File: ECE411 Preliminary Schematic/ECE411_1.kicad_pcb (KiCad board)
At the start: 2 copper layers, 12 parts, among them J2 Raspberry_Pi_4, M1 Motor_Servo, U1 XVF3800 (XM-014888-PC)

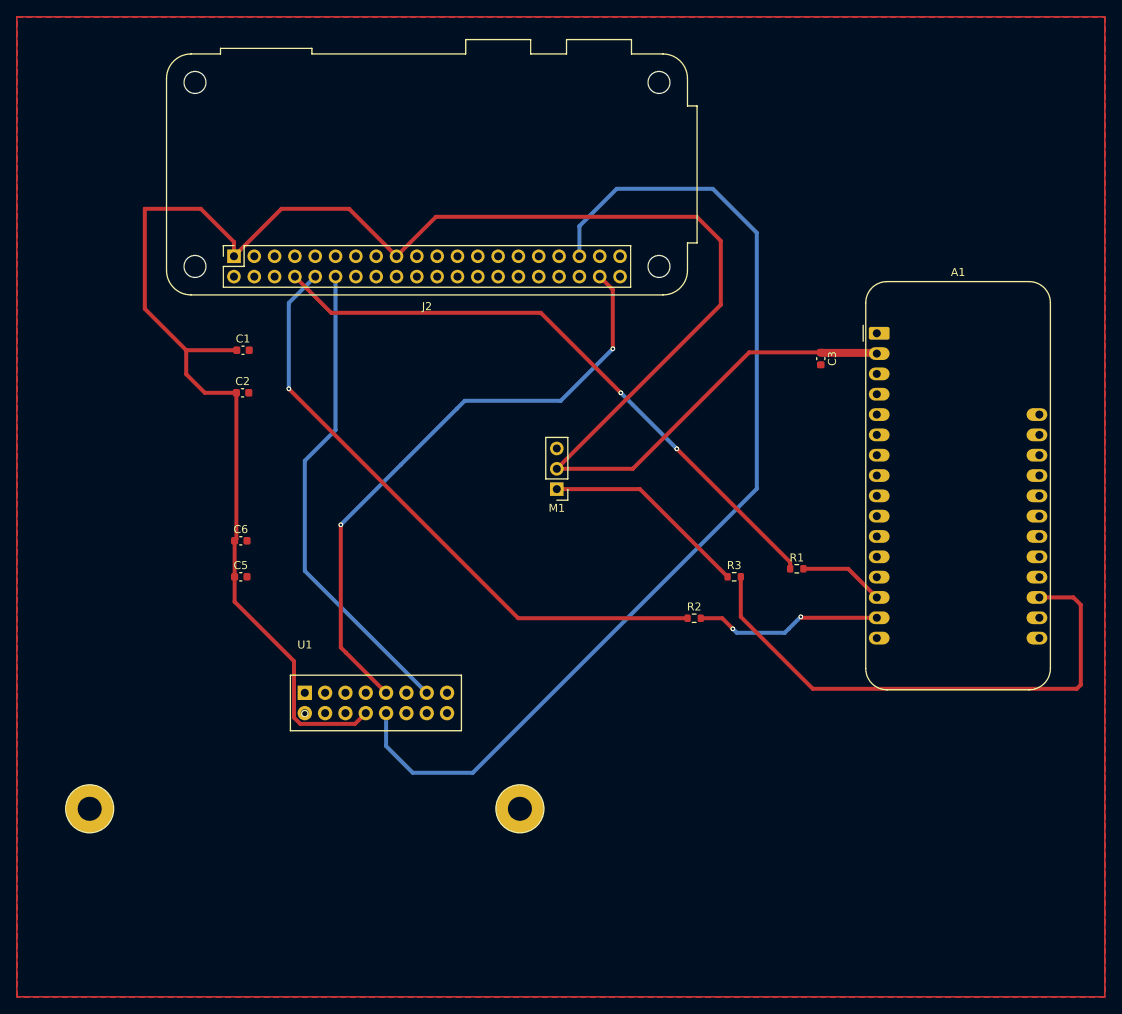
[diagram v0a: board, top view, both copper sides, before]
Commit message: update the PCB design to 3.0
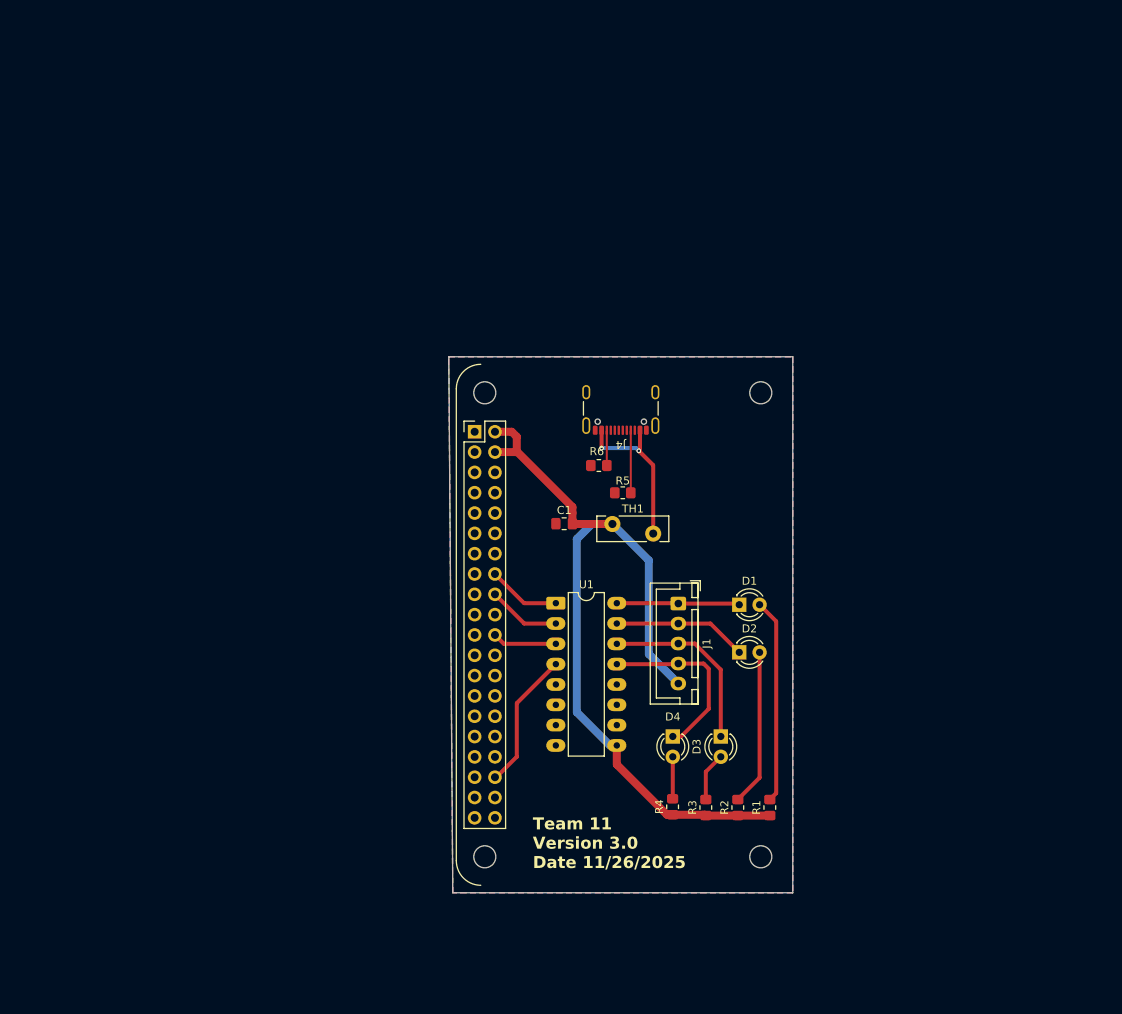
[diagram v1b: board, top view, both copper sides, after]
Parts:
- removed A1: Adafruit_Feather_HUZZAH32_ESP32, Module:Adafruit_Feather
- removed C2, C3, C6: 0.1uF, Capacitor_SMD:C_0603_1608Metric
- removed C5: 1uF, Capacitor_SMD:C_0603_1608Metric
- removed M1: Motor_Servo, Connector_PinHeader_2.54mm:PinHeader_1x03_P2.54mm_Vertical
- added ?: , , F.Cu at (141.0, 146.0)
- added ?: , , F.Cu at (141.0, 88.0)
- added D1: LED, LED_THT:LED_D3.0mm, F.Cu at (138.3, 114.5)
- added D2: LED, LED_THT:LED_D3.0mm, F.Cu at (138.3, 120.4)
- added D3: LED, LED_THT:LED_D3.0mm, F.Cu at (136.0, 131.0)
- added D4: LED, LED_THT:LED_D3.0mm, F.Cu at (130.0, 131.0)
- added J1: Conn_01x05, Connector_JST:JST_XH_B5B-XH-A_1x05_P2.50mm_Vertical, F.Cu at (130.7, 114.3)
- added J4: USB_C_Receptacle_USB2.0_16P, Connector_USB:USB_C_Receptacle_GCT_USB4105-xx-A_16P_TopMnt_Horizontal, F.Cu at (123.5, 89.0)
- added R4: 0.5k, Resistor_SMD:R_0805_2012Metric_Pad1.20x1.40mm_HandSolder, F.Cu at (130.0, 139.7)
- added R5: 5.1k, Resistor_SMD:R_0805_2012Metric_Pad1.20x1.40mm_HandSolder, F.Cu at (123.7, 100.5)
- added R6: 5.1k, Resistor_SMD:R_0805_2012Metric_Pad1.20x1.40mm_HandSolder, F.Cu at (120.8, 97.1)
- added TH1: Thermistor_PTC, Fuse:Fuse_Bourns_MF-RHT300, F.Cu at (122.5, 104.4)
- C1: value 1uF -> 100nF; footprint Capacitor_SMD:C_0603_1608Metric -> Capacitor_SMD:C_0805_2012Metric_Pad1.18x1.45mm_HandSolder
- J2: footprint Module:Raspberry_Pi_Zero_Socketed_THT_FaceDown_MountingHoles -> XVF_3800_Dock:rap5
- R1, R2, R3: value 100 -> 0.5k; footprint Resistor_SMD:R_0603_1608Metric -> Resistor_SMD:R_0805_2012Metric_Pad1.20x1.40mm_HandSolder
- U1: value XVF3800 (XM-014888-PC) -> ULN2003; footprint XVF_3800_Dock:XVF3800_Dock_2x8_Slot_M3 -> Package_DIP:DIP-16_W7.62mm_LongPads
- moved J2 51.2 mm to (101.3, 115.0), turned to 0 degrees
- moved C1 45.6 mm to (116.4, 104.4)
- moved U1 33.3 mm to (115.4, 114.3)
- moved R1 30.0 mm to (142.1, 139.8), turned to 90 degrees
- moved R3 29.1 mm to (134.1, 139.8), turned to 90 degrees
- moved R2 24.3 mm to (138.1, 139.8), turned to 90 degrees
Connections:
- C1 pad 1: +3V3 -> GND
- C1 pad 2: GND -> /VCC
- J2 pad 1: +3V3 -> unconnected-(J2-3V3-Pad1)_1
- J2 pad 10: PI_ESP_TX -> unconnected-(J2-GPIO15/UART_RXD-Pad10)
- J2 pad 12: CLK -> unconnected-(J2-GPIO18/SPI1_~{CE0}/PCM_CLK/PWM0-Pad12)
- J2 pad 16: unconnected-(J2-GPIO23/SDIO_CMD-Pad16) -> IN1
- J2 pad 17: +3V3 -> unconnected-(J2-3V3-Pad1)
- J2 pad 18: unconnected-(J2-GPIO24/SDIO_DAT0-Pad18) -> IN2
- J2 pad 2: unconnected-(J2-5V-Pad2) -> /VCC
- J2 pad 22: unconnected-(J2-GPIO25/SDIO_DAT1-Pad22) -> IN3
- J2 pad 35: DIRECTION -> unconnected-(J2-GPIO19/SPI1_MISO/PCM_FS-Pad35)
- J2 pad 36: unconnected-(J2-GPIO16/SPI1_~{CE2}-Pad36) -> IN4
- J2 pad 38: AUDIO_DATA -> unconnected-(J2-GPIO20/SPI1_MOSI/PCM_DIN/PWM1-Pad38)
- J2 pad 4: unconnected-(J2-5V-Pad2)_1 -> /VCC
- J2 pad 8: PI_ESP_RX -> unconnected-(J2-GPIO14/UART_TXD-Pad8)
- R1 pad 1: PI_ESP_RX -> /VCC
- R2 pad 1: PI_ESP_TX -> /VCC
- R3 pad 1: Net-(M1-PWM) -> /VCC
- U1 pad 1: unconnected-(U1-QSPI_D1/BOOTSEL-Pad1) -> IN1
- U1 pad 10: DIRECTION -> unconnected-(U1-O7-Pad10)
- U1 pad 11: (no net) -> unconnected-(U1-O6-Pad11)
- U1 pad 12: (no net) -> unconnected-(U1-O5-Pad12)
- U1 pad 13: CLK -> Net-(D4-K)
- U1 pad 14: unconnected-(U1-MCLK_INOUT-Pad14) -> Net-(D3-K)
- U1 pad 15: unconnected-(U1-XOUT-Pad15) -> Net-(D2-K)
- U1 pad 16: unconnected-(U1-XIN-Pad16) -> Net-(D1-K)
- U1 pad 2: unconnected-(U1-QSPI_D3-Pad2) -> IN2
- U1 pad 3: unconnected-(U1-QSPI_CS_N-Pad3) -> IN3
- U1 pad 4: unconnected-(U1-VDD-Pad4) -> IN4
- U1 pad 8: +3V3 -> GND
- U1 pad 9: AUDIO_DATA -> /VCC
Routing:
- net +3V3: track 256.8 -> 0.00 mm
- net DIRECTION: track 128.7 -> 0.00 mm
- net /VCC: track 0.00 -> 105.6 mm
- net PI_ESP_RX: track 77.5 -> 0.00 mm, vias 2 -> 0
- net PI_ESP_TX: track 77.1 -> 0.00 mm, vias 1 -> 0
- net AUDIO_DATA: track 76.2 -> 0.00 mm, vias 2 -> 0
- net Net-(D3-A): track 67.0 -> 6.12 mm
- net CLK: track 59.9 -> 0.00 mm
- net Net-(M1-PWM): track 25.9 -> 0.00 mm
- net Net-(D3-K): track 0.00 -> 22.7 mm
- net Net-(D4-K): track 0.00 -> 22.6 mm
- net Net-(J4-VBUS-PadA4): track 0.00 -> 20.7 mm, vias 0 -> 2
- net IN4: track 0.00 -> 17.4 mm
- net Net-(D2-K): track 0.00 -> 16.8 mm
- net Net-(D1-K): track 0.00 -> 15.9 mm
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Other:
- board outline added: 43 x 67 mm
- board text added: "Team 11 Version 3.0 Date 11/26/2025"
